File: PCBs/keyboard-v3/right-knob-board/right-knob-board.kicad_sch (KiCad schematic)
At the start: 11 parts, among them M1 2206-100T, SW1 SW_DIP_x01, SW2 SW_DIP_x01, SW3 SW_DIP_x01, U1 STM32G0C1CEUx

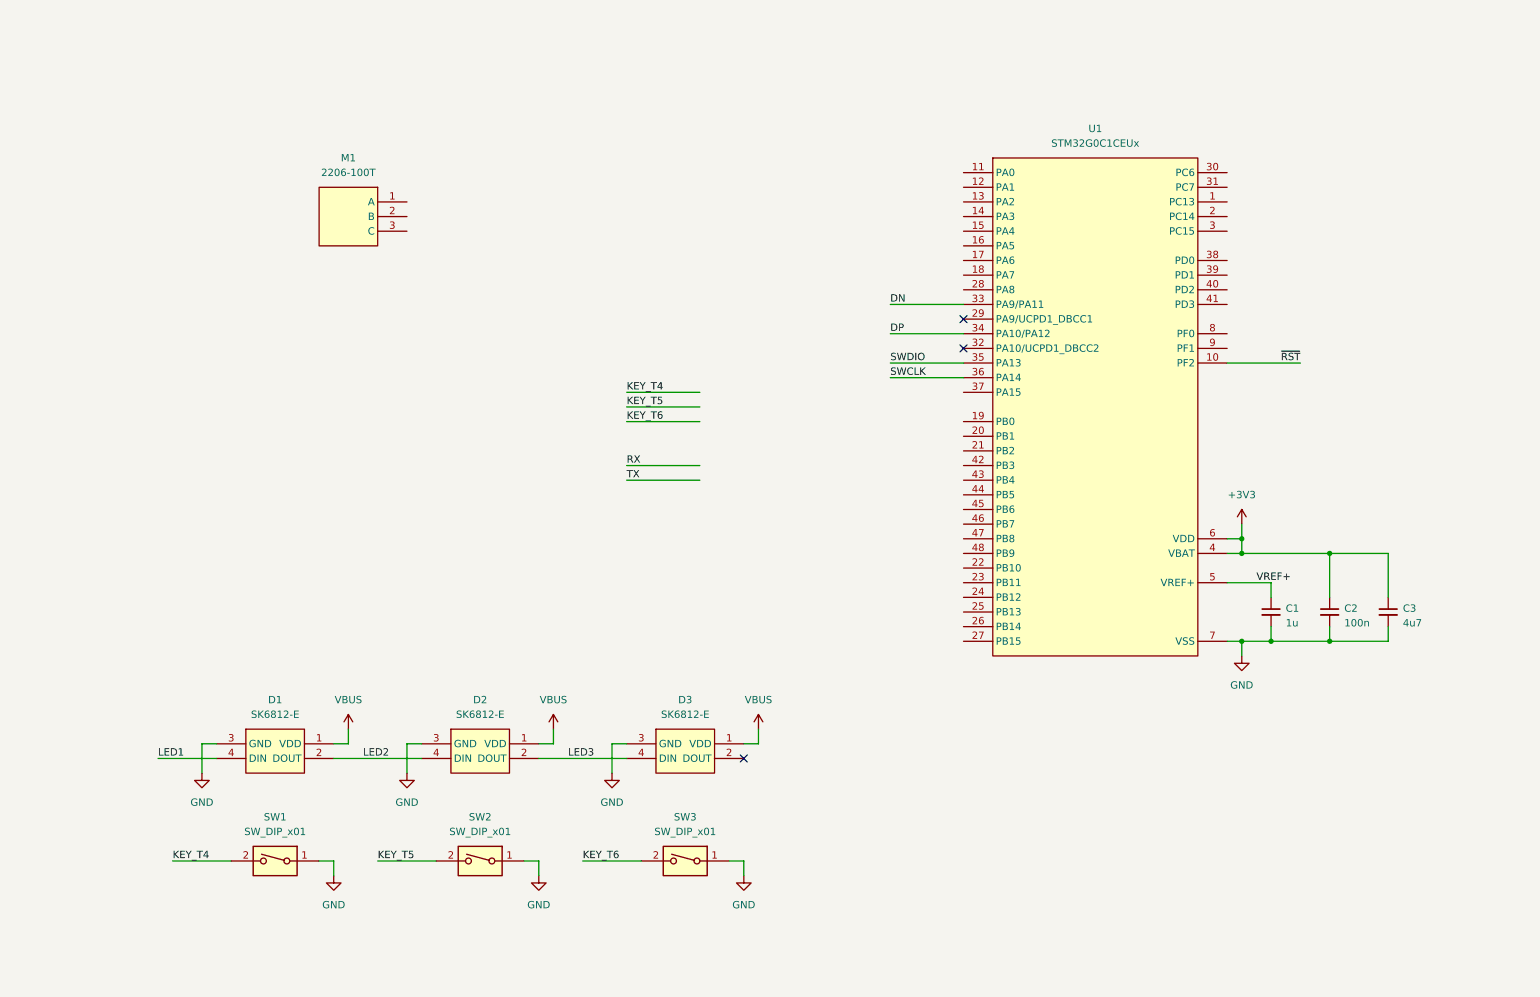
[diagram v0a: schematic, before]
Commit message: Key board schematic done and layout half done
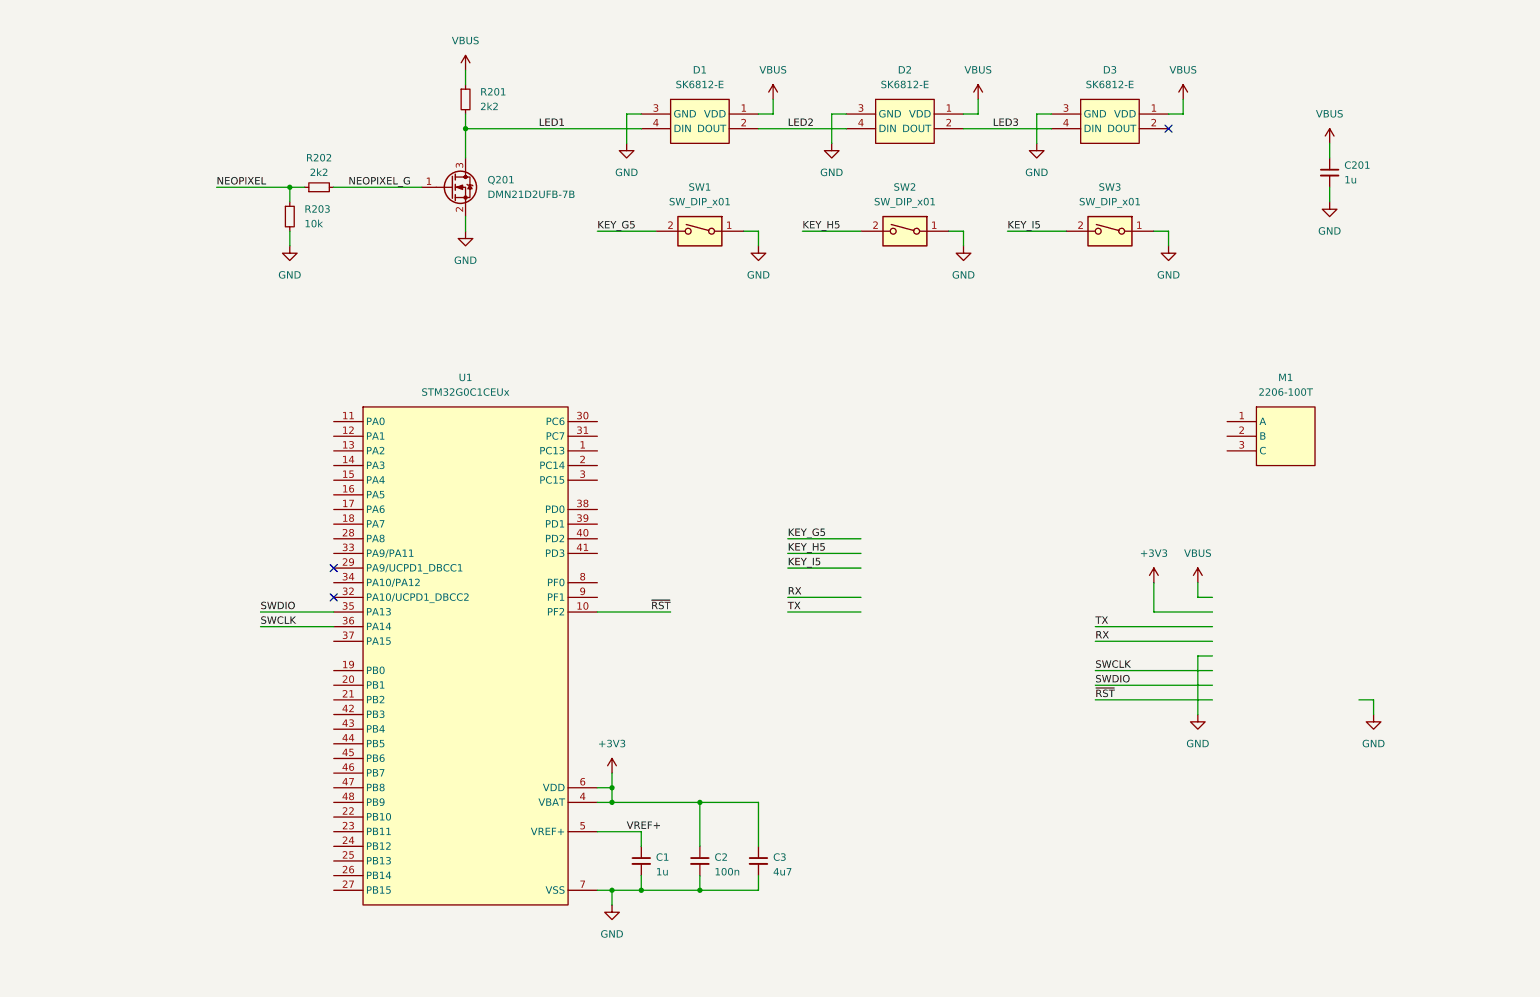
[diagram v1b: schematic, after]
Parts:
- added C201: 1u, project_footprints:C_0402, symbol DEV:C_SMALL
- added Q201: DMN21D2UFB-7B, project_footprints:DMN21D2UFB7B, symbol MOSFET:DMN21D2UFB-7B
- added R201, R202: 2k2, symbol DEV:R_SMALL
- added R203: 10k, symbol DEV:R_SMALL
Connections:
- net GND: now also C201.2, Q201.2 (S), R203.2
- net LED1: now also Q201.3 (D), R201.2
- net VBUS: now also C201.1, R201.1
- net DN: no longer names the net of U1.33 (PA9/PA11)
- net DP: no longer names the net of U1.34 (PA10/PA12)
- net KEY_T4 renamed KEY_G5
- net KEY_T5 renamed KEY_H5
- net KEY_T6 renamed KEY_I5
- new net NEOPIXEL: R202.1, R203.1
- new net NEOPIXEL_G: Q201.1 (G), R202.2
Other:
- moved on the sheet: C1, C2, C3, D1, D2, D3, M1, SW1, SW2, SW3, U1

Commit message: Right daughter boards finished
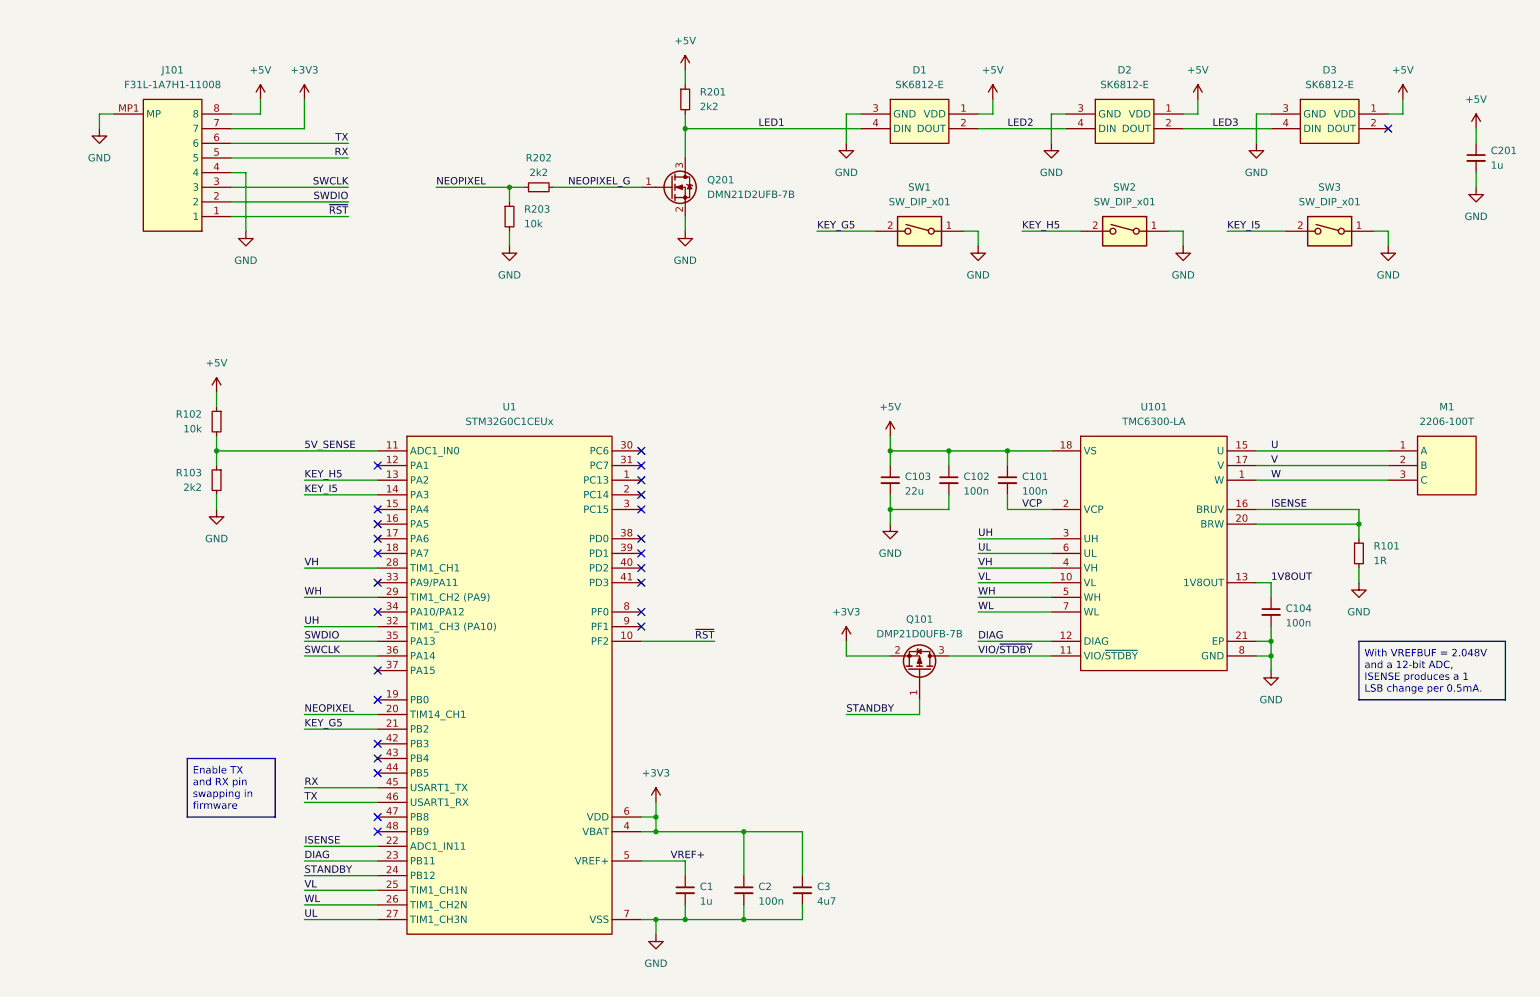
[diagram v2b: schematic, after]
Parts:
- added C101, C102, C104: 100n, project_footprints:C_0402, symbol DEV:C_SMALL
- added C103: 22u, project_footprints:C_0603, symbol DEV:C_SMALL
- added J101: F31L-1A7H1-11008, project_footprints:F31L-1A7H1-11008, symbol CONN-FPC:F31L-1A7H1-11008
- added Q101: DMP21D0UFB-7B, project_footprints:DMP21D0UFB7B, symbol MOSFET:DMP21D0UFB-7B
- added R101: 1R, project_footprints:R_0402, symbol DEV:R_SMALL
- added R102: 10k, project_footprints:R_0402, symbol DEV:R_SMALL
- added R103: 2k2, project_footprints:R_0402, symbol DEV:R_SMALL
- added U101: TMC6300-LA, project_footprints:QFN40P300X300X90-21N, symbol MOTOR-DRIVER:TMC6300-LA
- R201, R202, R203: footprint (none) -> project_footprints:R_0402
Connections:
- net +3V3: now also J101.7, Q101.2 (S)
- net GND: now also C102.2, C103.2, C104.2, J101.4, J101.MP1 (MP), J101.MP2 (MP), R101.2, R103.2, U101.14 (GND), U101.21 (EP), U101.8 (GND), U101.9 (GND)
- net KEY_G5: now also U1.21 (PB2)
- net KEY_H5: now also U1.13 (PA2)
- net KEY_I5: now also U1.14 (PA3)
- net NEOPIXEL: now also U1.20 (PB1)
- net RX: now also U1.45 (PB6), J101.5
- net SWCLK: now also J101.3
- net SWDIO: now also J101.2
- net TX: now also U1.46 (PB7), J101.6
- net ~{RST}: now also J101.1
- net U: now reaches M1.1 (A)
- net U: now also U101.15 (U)
- net V: now reaches M1.2 (B)
- net V: now also U101.17 (V)
- net W: now reaches M1.3 (C)
- net W: now also U101.1 (W)
- net 5V_SENSE: now reaches U1.11 (PA0)
- net 5V_SENSE: now also R102.2, R103.1
- net ISENSE: now reaches U1.22 (PB10)
- net ISENSE: now also R101.1, U101.16 (BRUV), U101.20 (BRW)
- net DIAG: now reaches U1.23 (PB11)
- net DIAG: now also U101.12 (DIAG)
- net STANDBY: now reaches U1.24 (PB12)
- net STANDBY: now also Q101.1 (G)
- net VL: now reaches U1.25 (PB13)
- net VL: now also U101.10 (VL)
- net WL: now reaches U1.26 (PB14)
- net WL: now also U101.7 (WL)
- net UL: now reaches U1.27 (PB15)
- net UL: now also U101.6 (UL)
- net VH: now reaches U1.28 (PA8)
- net VH: now also U101.4 (VH)
- net WH: now reaches U1.29 (PA9/UCPD1_DBCC1)
- net WH: now also U101.5 (WH)
- net UH: now reaches U1.32 (PA10/UCPD1_DBCC2)
- net UH: now also U101.3 (UH)
- net VBUS renamed +5V
- net +5V: now also C101.1, C102.1, C103.1, J101.8, R102.1, U101.18 (VS)
- new net 1V8OUT: C104.1, U101.13 (1V8OUT)
- new net VCP: C101.2, U101.2 (VCP)
- new net VIO/~{STDBY}: Q101.3 (D), U101.11 (VIO/~{STDBY})
- no-connect marks 3 -> 26
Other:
- moved on the sheet: C1, C2, C201, C3, D1, D2, D3, M1, Q201, R201, R202, R203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

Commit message: Added debug-breakout board, progress on right side schematics & layout
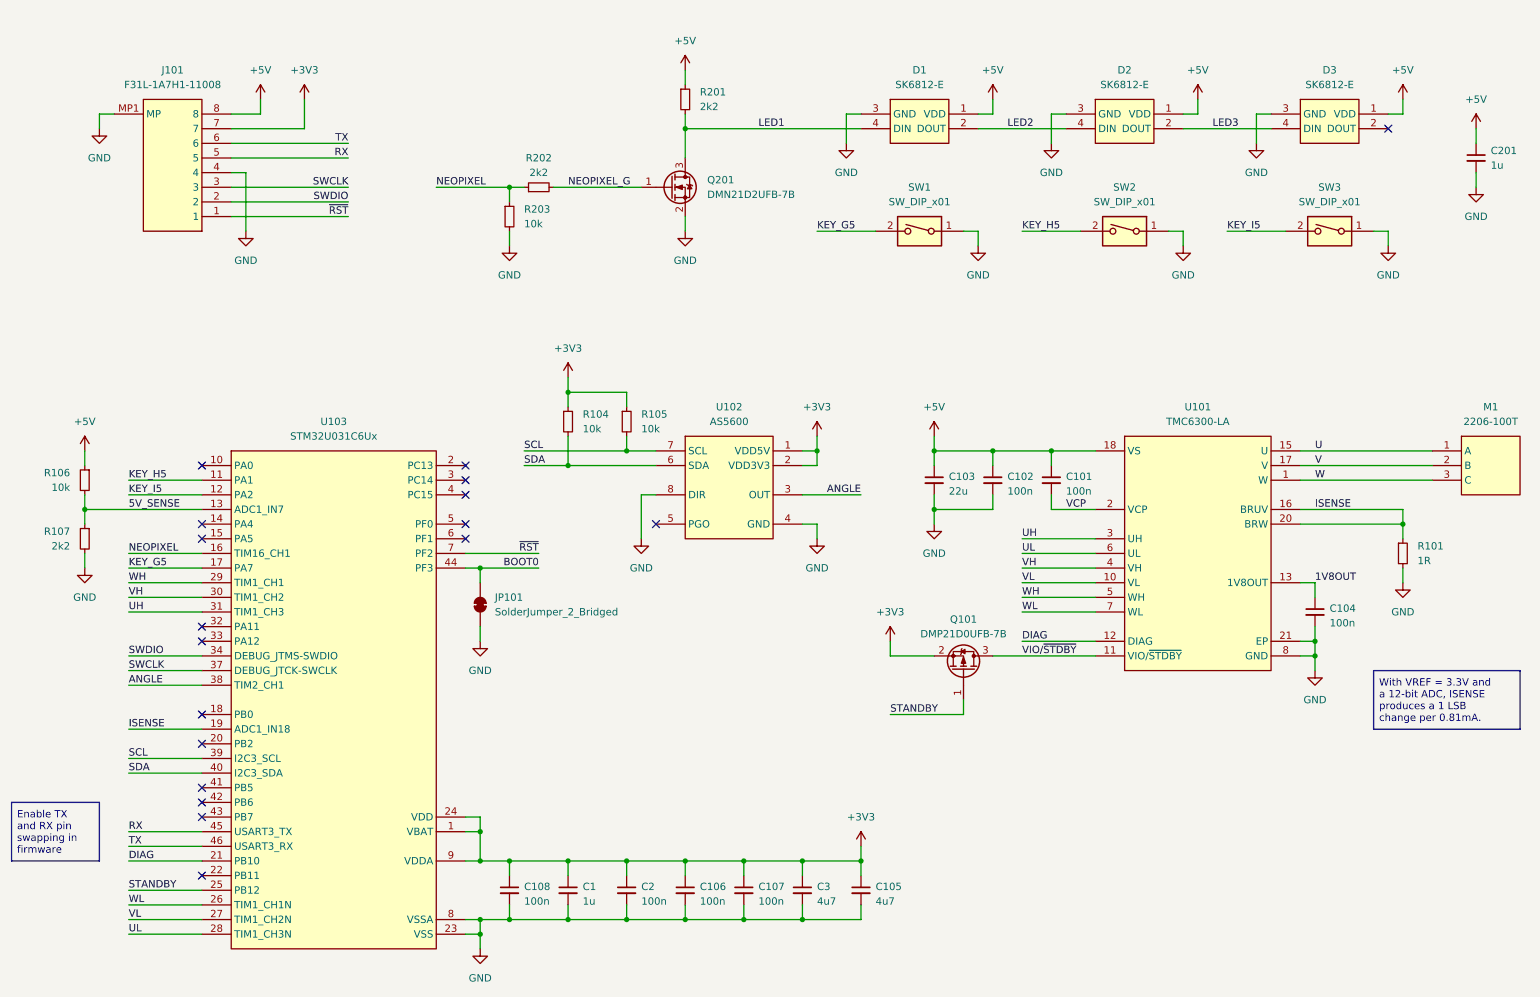
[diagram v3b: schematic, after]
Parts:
- removed R102: 10k, project_footprints:R_0402, symbol DEV:R_SMALL
- removed R103: 2k2, project_footprints:R_0402, symbol DEV:R_SMALL
- removed U1: STM32G0C1CEUx, project_footprints:QFN50P700X700X60-49N-D, symbol STM32:STM32G0C1CEUx
- added C105: 4u7, project_footprints:C_0402, symbol DEV:C_SMALL
- added C106, C107, C108: 100n, project_footprints:C_0402, symbol DEV:C_SMALL
- added JP101: SolderJumper_2_Bridged, Jumper:SolderJumper-2_P1.3mm_Bridged_RoundedPad1.0x1.5mm, symbol Jumper:SolderJumper_2_Bridged
- added R104, R105, R106: 10k, project_footprints:R_0402, symbol DEV:R_SMALL
- added R107: 2k2, project_footprints:R_0402, symbol DEV:R_SMALL
- added U102: AS5600, project_footprints:as5600-rear-magnet, symbol ENC:AS5600
- added U103: STM32U031C6Ux, project_footprints:QFN50P700X700X60-49N-D, symbol STM32:STM32U031C6Ux
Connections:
- net VREF+ is gone; now on net +3V3: C1.1
- net +3V3: now also C105.1, C106.1, C107.1, C108.1, R104.1, R105.1, U102.1 (VDD5V), U102.2 (VDD3V3), U103.1 (VBAT), U103.24 (VDD), U103.36 (VDD), U103.48 (VDD), U103.9 (VDDA)
- net +5V: now also R106.1
- net 5V_SENSE: now also R106.2, R107.1, U103.13 (PA3)
- net DIAG: now also U103.21 (PB10)
- net GND: now also C105.2, C106.2, C107.2, C108.2, JP101.1 (A), R107.2, U102.4 (GND), U102.8 (DIR), U103.23 (VSS), U103.35 (VSS), U103.47 (VSS), U103.49 (VSS), U103.8 (VSSA)
- net ISENSE: now also U103.19 (PB1)
- net KEY_G5: now also U103.17 (PA7)
- net KEY_H5: now also U103.11 (PA1)
- net KEY_I5: now also U103.12 (PA2)
- net NEOPIXEL: now also U103.16 (PA6)
- net RX: now also U103.45 (PB8)
- net STANDBY: now also U103.25 (PB12)
- net SWCLK: now also U103.37 (PA14)
- net SWDIO: now also U103.34 (PA13)
- net TX: now also U103.46 (PB9)
- net UH: now also U103.31 (PA10)
- net UL: now also U103.28 (PB15)
- net VH: now also U103.30 (PA9)
- net VL: now also U103.27 (PB14)
- net WH: now also U103.29 (PA8)
- net WL: now also U103.26 (PB13)
- net ~{RST}: now also U103.7 (PF2)
- new net ANGLE: U102.3 (OUT), U103.38 (PA15)
- new net BOOT0: JP101.2 (B), U103.44 (PF3)
- new net SCL: R105.2, U102.7 (SCL), U103.39 (PB3)
- new net SDA: R104.2, U102.6 (SDA), U103.40 (PB4)
- no-connect marks 26 -> 18
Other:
- moved on the sheet: C1, C101, C102, C103, C104, C2, M1, Q101, R101, U101

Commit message: Added power gate to AS5600 to reduce its sleep current
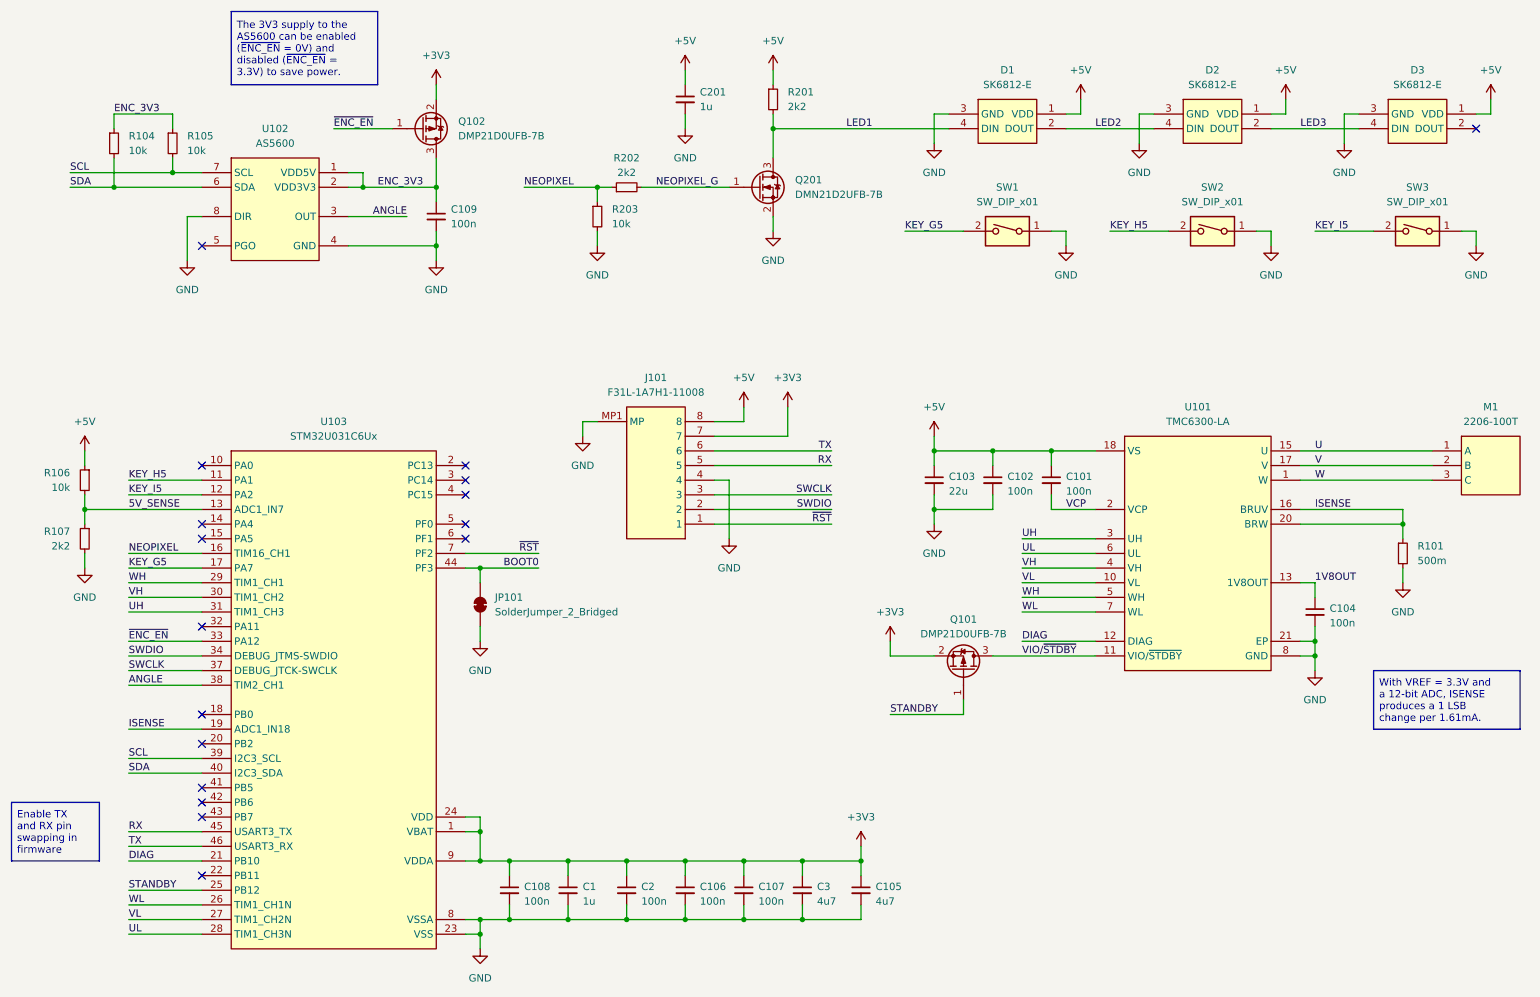
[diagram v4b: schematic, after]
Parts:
- added C109: 100n, project_footprints:C_0402, symbol DEV:C_SMALL
- added Q102: DMP21D0UFB-7B, project_footprints:DMP21D0UFB7B, symbol MOSFET:DMP21D0UFB-7B
- R101: value 1R -> 500m
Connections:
- net +3V3: now also Q102.2 (S); no longer R104.1, R105.1, U102.1 (VDD5V), U102.2 (VDD3V3)
- net GND: now also C109.2
- net ~{ENC_EN}: now reaches U103.33 (PA12)
- net ~{ENC_EN}: now also Q102.1 (G)
- new net ENC_3V3: C109.1, Q102.3 (D), R104.1, R105.1, U102.1 (VDD5V), U102.2 (VDD3V3)
- no-connect marks 18 -> 17
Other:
- moved on the sheet: C201, D1, D2, D3, J101, Q201, R104, R105, R201, R202, R203, SW1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
